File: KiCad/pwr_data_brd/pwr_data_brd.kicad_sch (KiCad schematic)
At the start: 30 parts, among them J7 USB_A, J8 USB_A, Q1 DMP4047LFDE-7, U13 MAX8510EXK30T, U14 TPS62133RGTR

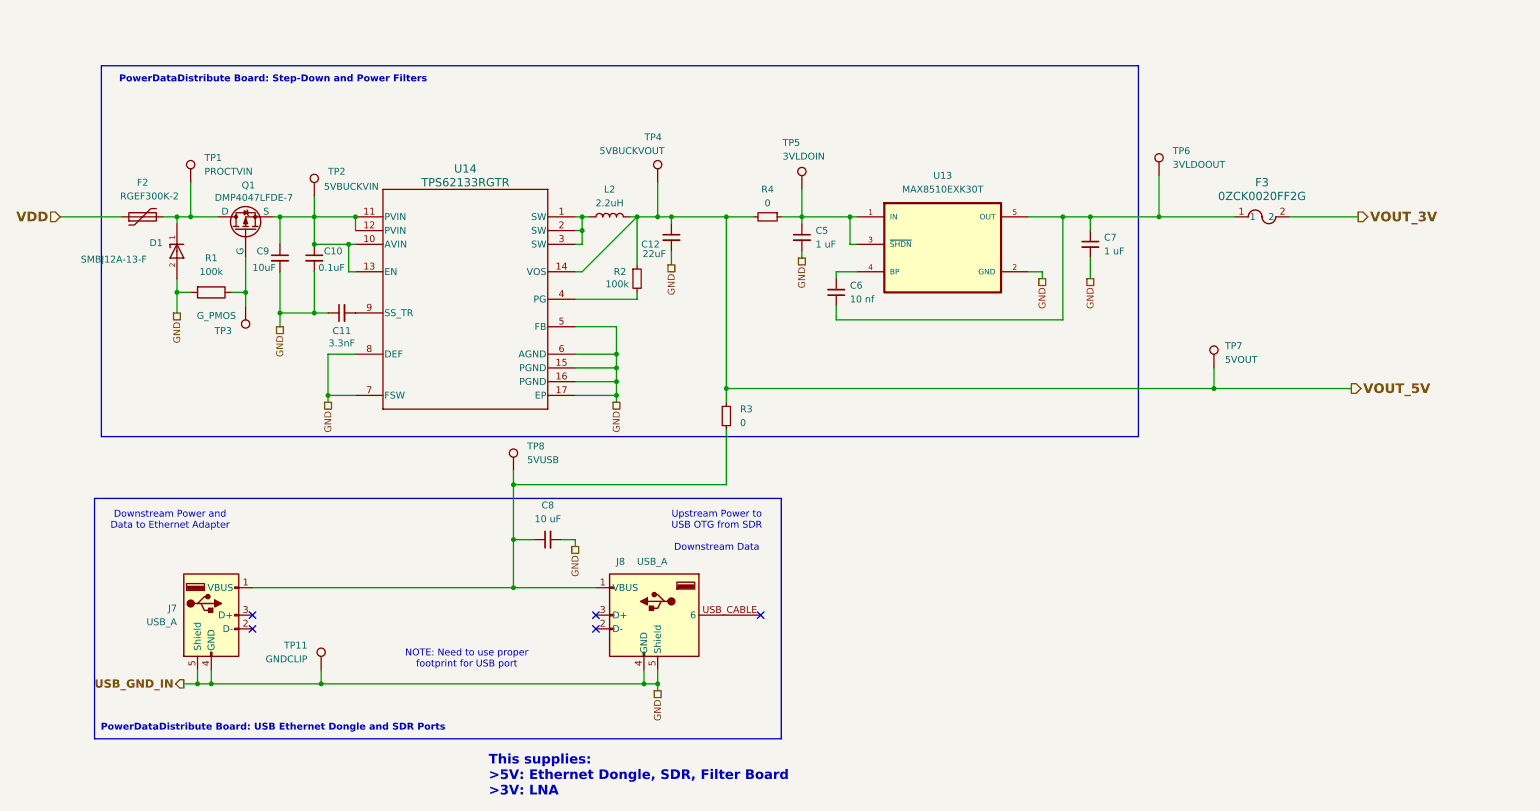
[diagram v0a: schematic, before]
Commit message: Fix power board symbols and nets, added project specific libs
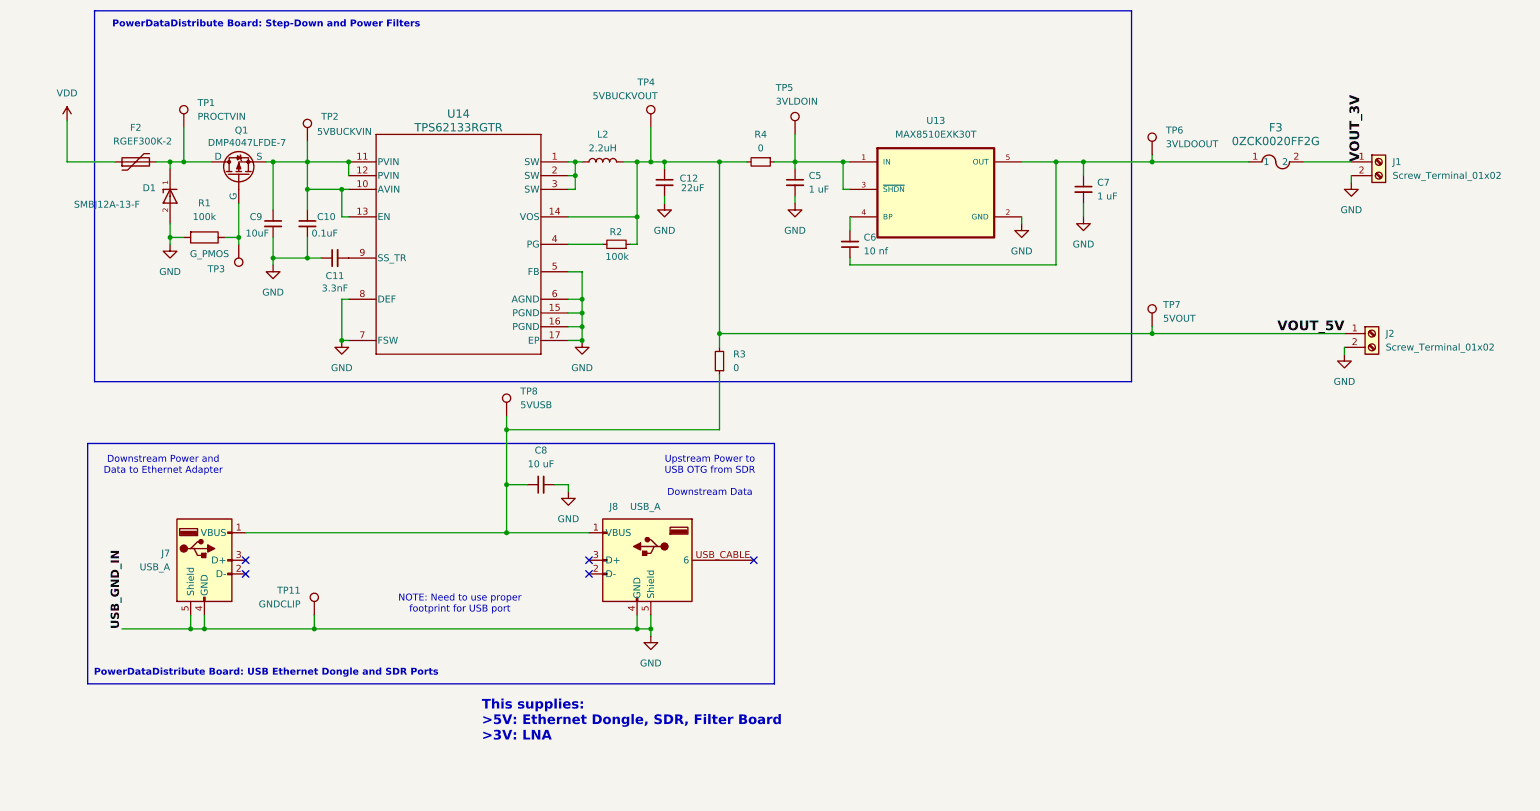
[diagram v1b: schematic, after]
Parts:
- added J1, J2: Screw_Terminal_01x02, symbol Connector:Screw_Terminal_01x02
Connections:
- net GND: now also J1.2 (Pin_2), J2.2 (Pin_2)
- net VOUT_3V: now also J1.1 (Pin_1)
- net VOUT_5V: now also J2.1 (Pin_1)
